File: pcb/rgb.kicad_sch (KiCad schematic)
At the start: 29 parts, among them J1 Conn_02x08_Odd_Even, J2 Conn_01x02, J3 Conn_01x02_Pin, J4 TYPE-C-31-M-12, J5 TF-01A, J6 Conn_01x02_Pin, U4 SW, U5 ESP32-WROOM-32E, U7 CH340C, U8 SPX3819M5-L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

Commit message: pcb: exploration
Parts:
- removed J3, J6: Conn_01x02_Pin, symbol Connector:Conn_01x02_Pin
- added J3, J7: B4PS-VH, Connector_PinSocket_2.54mm:PinSocket_1x04_P2.54mm_Vertical, symbol Connector:Conn_01x04_Pin
- J1: footprint Pin_Headers:Pin_Header_Angled_2x08_Pitch2.54mm -> Connector_PinSocket_2.54mm:PinSocket_2x08_P2.54mm_Vertical
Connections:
- net +5V: now also J7.1 (Pin_1), J7.2 (Pin_2)
- net GND: now also J3.3 (Pin_3), J3.4 (Pin_4), J7.3 (Pin_3), J7.4 (Pin_4)
- net Stepdown_b/v_out: now also J3.1 (Pin_1), J3.2 (Pin_2)
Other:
- moved on the sheet: C7, C8, R5, R7, U8

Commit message: initial routing done
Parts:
- removed R12: 10k, Resistors_SMD:R_0805, symbol Device:R
- removed R9: 10k, Resistor_SMD:R_0603_1608Metric, symbol Device:R
- C5: footprint Capacitors_SMD:C_0805 -> Capacitor_SMD:C_0603_1608Metric
- J2: footprint Pin_Headers:Pin_Header_Angled_1x02_Pitch2.54mm -> Connector_PinHeader_2.54mm:PinHeader_1x02_P2.54mm_Horizontal
- J5: footprint (none) -> espirgbani:TF-01A
- R4, R6: footprint Resistors_SMD:R_0805 -> Resistor_SMD:R_0603_1608Metric
- U4: value SW -> WIFI; footprint myStuff:EVQQ2 -> espirgbani:EVQQ2
- U9: footprint crtdriver2:SSOP-10-1EP_3.9x4.9mm_P1.00mm -> espirgbani:SSOP-10-1EP_3.9x4.9mm_P1.00mm
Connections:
- net USB_D_N is gone; now on net USB_N: U7.6 (UD-)
- net USB_D_P is gone; now on net USB_P: U7.5 (UD+)
- net +3.3V: now also C4.1, J2.2 (Pin_2), J5.4 (VDD)
- net +3V3: no longer C4.1, J2.1 (Pin_1), J5.4 (VDD)
- net A: now also U5.30 (IO18); no longer U5.29 (IO5)
- net B: now also U5.29 (IO5); no longer U5.30 (IO18)
- net CLK: now also U5.14 (IO12); no longer U5.36 (IO22)
- net at C5.1, R6.1, U5.4 (SENSOR_VP): now also J2.1 (Pin_1); no longer J2.2 (Pin_2)
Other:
- note added: "Light sensor ALS-PDIC144-6C/L378"
- note removed: "Photo resistor"
- moved on the sheet: J2, U4

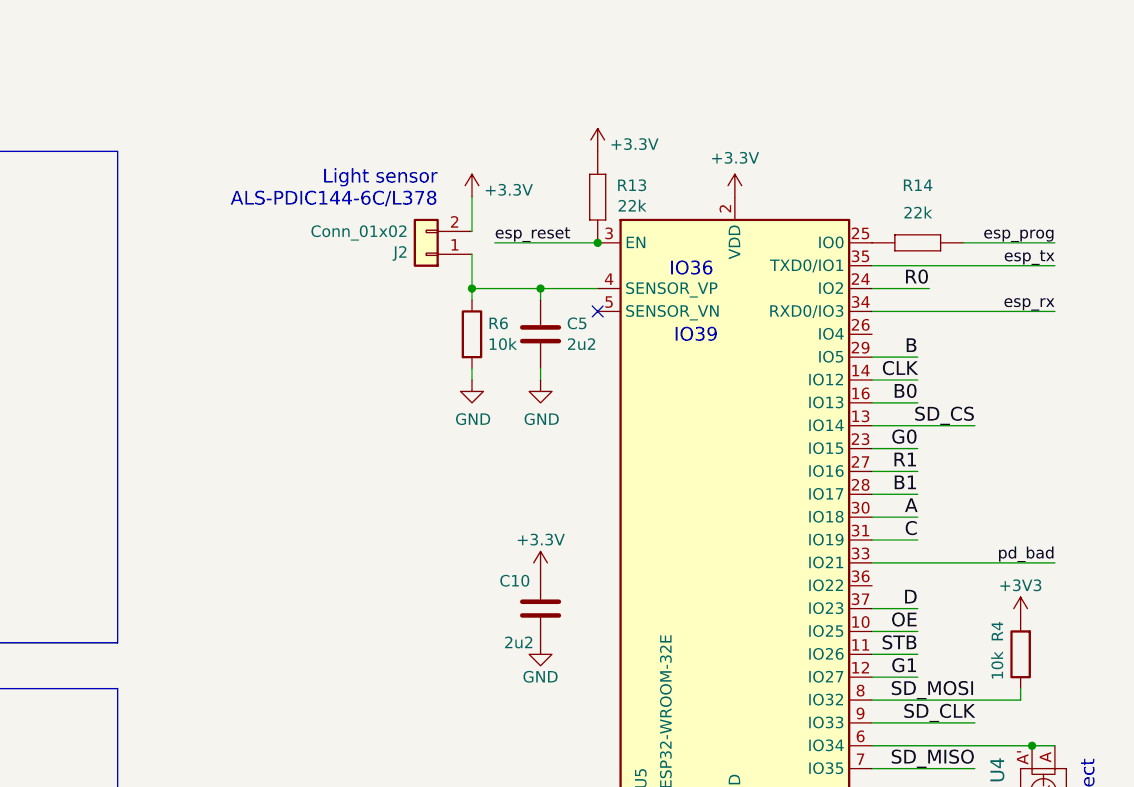
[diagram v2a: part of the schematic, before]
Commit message: turn esp by 90 deg
rip-up, re-route
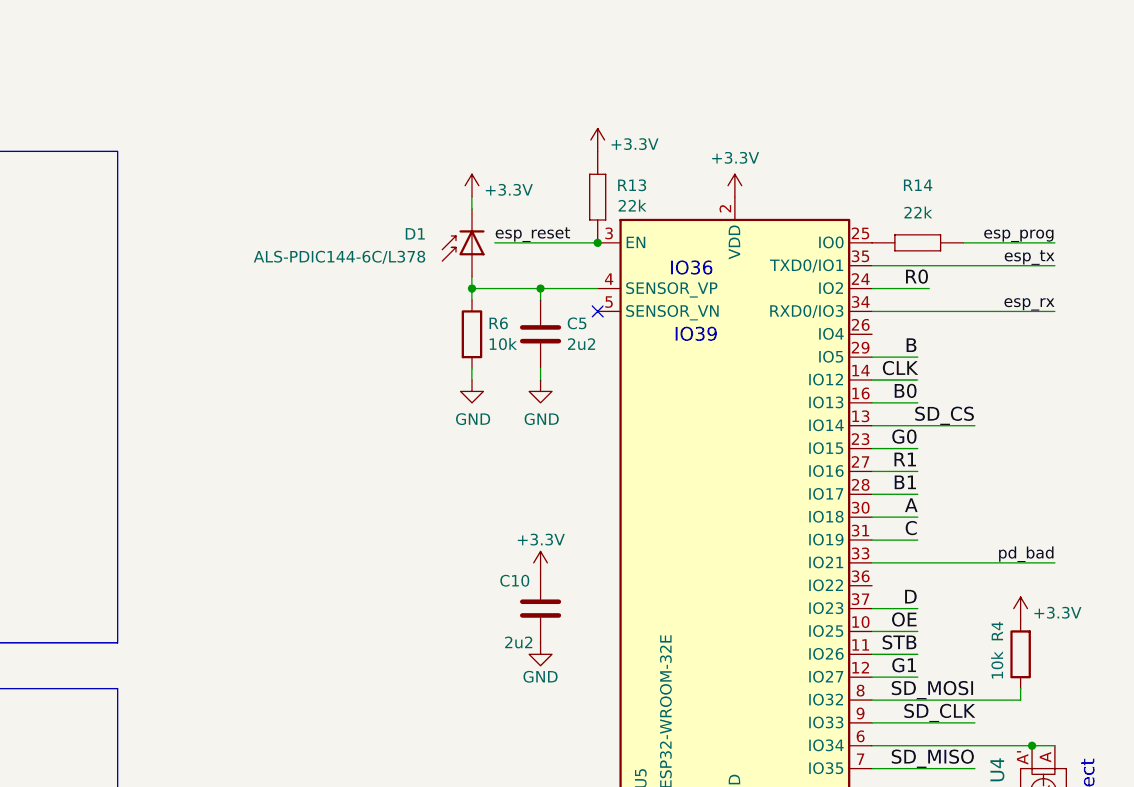
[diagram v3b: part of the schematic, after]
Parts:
- removed J2: Conn_01x02, Connector_PinHeader_2.54mm:PinHeader_1x02_P2.54mm_Horizontal, symbol Connector_Generic:Conn_01x02
- added D1: ALS-PDIC144-6C/L378, LED_THT:LED_D3.0mm_Horizontal_O3.81mm_Z6.0mm, symbol Device:D_Photo
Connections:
- net +3V3 is gone; now on net +3.3V: R4.2
- net +3.3V: now also D1.1 (K)
- net at C5.1, R6.1, U5.4 (SENSOR_VP): now also D1.2 (A)
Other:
- note removed: "Light sensor ALS-PDIC144-6C/L378"
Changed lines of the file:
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@@
 	(wire
 		(pts
-			(xy 203.2 82.55) (xy 203.2 86.36)
-		)
-		(stroke
-			(width 0)
-			(type default)
-		)
-	)
-	(wire
-		(pts
 			(xy 266.7 154.94) (xy 265.43 154.94)
 		)
@@
 	(wire
 		(pts
+			(xy 203.2 82.55) (xy 203.2 83.82)
+		)
+		(stroke
+			(width 0)
+			(type default)
+		)
+	)
+	(wire
+		(pts
 			(xy 247.65 44.45) (xy 242.57 44.45)
 		)
@@
 	(wire
 		(pts
-			(xy 203.2 88.9) (xy 203.2 92.71)
+			(xy 203.2 91.44) (xy 203.2 92.71)
 		)
 		(stroke
@@
 		)
 	)
-	(text "Light sensor\nALS-PDIC144-6C/L378"
-		(exclude_from_sim no)
-		(at 199.39 83.82 0)
-		(effects
-			(font
-				(size 1.524 1.524)
-			)
-			(justify right bottom)
-		)
-	)
 	(label "B"
 		(at 266.7 41.91 180)
@@
 	)
 	(symbol
-		(lib_id "power:+3.3V")
-		(at 264.16 129.54 0)
-		(unit 1)
-		(exclude_from_sim no)
-		(in_bom yes)
-		(on_board yes)
-		(dnp no)
-		(property "Reference" "#PWR019"
-			(at 264.16 133.35 0)
-			(effects
-				(font
-					(size 1.27 1.27)
-				)
-				(hide yes)
-			)
-		)
-		(property "Value" "+3V3"
-			(at 264.16 125.73 0)
-			(effects
-				(font
-					(size 1.27 1.27)
-				)
-			)
-		)
-		(property "Footprint" ""
-			(at 264.16 129.54 0)
-			(effects
-				(font
-					(size 1.27 1.27)
-				)
-				(hide yes)
-			)
-		)
-		(property "Datasheet" ""
-			(at 264.16 129.54 0)
-			(effects
-				(font
-					(size 1.27 1.27)
-				)
-				(hide yes)
-			)
-		)
-		(property "Description" ""
-			(at 264.16 129.54 0)
-			(effects
-				(font
-					(size 1.27 1.27)
-				)
-				(hide yes)
-			)
-		)
-		(pin "1"
-		)
-		(instances
-			(project "rgb"
-				(path "/e2cadc20-e108-4c6f-b279-00d9d28fa9da"
-					(reference "#PWR019")
-					(unit 1)
-				)
-			)
-		)
-	)
-	(symbol
 		(lib_id "rgb-rescue:TACTILE-myStuff")
 		(at 266.7 148.59 270)
@@
 	)
 	(symbol
-		(lib_id "Connector_Generic:Conn_01x02")
-		(at 198.12 88.9 180)
-		(unit 1)
-		(exclude_from_sim no)
-		(in_bom yes)
-		(on_board yes)
-		(dnp no)
-		(property "Reference" "J2"
-			(at 196.088 88.6968 0)
-			(effects
-				(font
-					(size 1.27 1.27)
-				)
-				(justify left)
-			)
-		)
-		(property "Value" "Conn_01x02"
-			(at 196.088 86.3854 0)
-			(effects
-				(font
-					(size 1.27 1.27)
-				)
-				(justify left)
-			)
-		)
-		(property "Footprint" "Connector_PinHeader_2.54mm:PinHeader_1x02_P2.54mm_Horizontal"
-			(at 198.12 88.9 0)
-			(effects
-				(font
-					(size 1.27 1.27)
-				)
-				(hide yes)
-			)
-		)
-		(property "Datasheet" ""
-			(at 198.12 88.9 0)
-			(effects
-				(font
-					(size 1.27 1.27)
-				)
-				(hide yes)
-			)
-		)
-		(property "Description" ""
-			(at 198.12 88.9 0)
-			(effects
-				(font
-					(size 1.27 1.27)
-				)
-				(hide yes)
-			)
-		)
-		(pin "1"
-		)
-		(pin "2"
-		)
-		(instances
-			(project "rgb"
-				(path "/e2cadc20-e108-4c6f-b279-00d9d28fa9da"
-					(reference "J2")
-					(unit 1)
-				)
-			)
-		)
-	)
-	(symbol
 		(lib_id "power:GND")
 		(at 133.35 95.25 0)
@@
 	)
 	(symbol
+		(lib_id "Device:D_Photo")
+		(at 203.2 88.9 90)
+		(mirror x)
+		(unit 1)
+		(exclude_from_sim no)
+		(in_bom yes)
+		(on_board yes)
+		(dnp no)
+		(property "Reference" "D1"
+			(at 198.12 86.6774 90)
+			(effects
+				(font
+					(size 1.27 1.27)
+				)
+				(justify left)
+			)
+		)
+		(property "Value" "ALS-PDIC144-6C/L378"
+			(at 198.12 89.2174 90)
+			(effects
+				(font
+					(size 1.27 1.27)
+				)
+				(justify left)
+			)
+		)
+		(property "Footprint" "LED_THT:LED_D3.0mm_Horizontal_O3.81mm_Z6.0mm"
+			(at 203.2 87.63 0)
+			(effects
+				(font
+					(size 1.27 1.27)
+				)
+				(hide yes)
+			)
+		)
+		(property "Datasheet" "~"
+			(at 203.2 87.63 0)
+			(effects
+				(font
+					(size 1.27 1.27)
+				)
+				(hide yes)
+			)
+		)
+		(property "Description" "Photodiode"
+			(at 203.2 88.9 0)
+			(effects
+				(font
+					(size 1.27 1.27)
+				)
+				(hide yes)
+			)
+		)
+		(pin "2"
+		)
+		(pin "1"
+		)
+		(instances
+			(project "rgb"
+				(path "/e2cadc20-e108-4c6f-b279-00d9d28fa9da"
+					(reference "D1")
+					(unit 1)
+				)
+			)
+		)
+	)
+	(symbol
 		(lib_id "power:+3.3V")
 		(at 203.2 82.55 0)
@@
 					(unit 1)
 				)
+			)
+		)
+	)
+	(symbol
+		(lib_id "power:+3.3V")
+		(at 264.16 129.54 0)
+		(unit 1)
+		(exclude_from_sim no)
+		(in_bom yes)
+		(on_board yes)
+		(dnp no)
+		(property "Reference" "#PWR019"
+			(at 264.16 133.35 0)
+			(effects
+				(font
+					(size 1.27 1.27)
+				)
+				(hide yes)
+			)
+		)
+		(property "Value" "+3.3V"
+			(at 268.224 128.778 0)
+			(effects
+				(font
+					(size 1.27 1.27)
+				)
+			)
+		)
+		(property "Footprint" ""
+			(at 264.16 129.54 0)
+			(effects
+				(font
+					(size 1.27 1.27)
+				)
+				(hide yes)
+			)
+		)
+		(property "Datasheet" ""
+			(at 264.16 129.54 0)
+			(effects
+				(font
+					(size 1.27 1.27)
+				)
+				(hide yes)
+			)
+		)
+		(property "Description" "Power symbol creates a global label with name \"+3.3V\""
+			(at 264.16 129.54 0)
+			(effects
+				(font
+					(size 1.27 1.27)
+				)
+				(hide yes)
+			)
+		)
+		(pin "1"
+		)
+		(instances
+			(project "rgb"
+				(path "/e2cadc20-e108-4c6f-b279-00d9d28fa9da"
+					(reference "#PWR019")
+					(unit 1)
+				)

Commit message: optimize pinout
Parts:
- C4: value 10u -> 2u2; footprint Capacitor_SMD:C_1206_3216Metric -> Capacitor_SMD:C_0603_1608Metric; JLCPN C13585 -> (none)
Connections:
- net A: now also U5.27 (IO16); no longer U5.30 (IO18)
- net B: now also U5.28 (IO17); no longer U5.29 (IO5)
- net B0: now also U5.33 (IO21); no longer U5.16 (IO13)
- net B1: now also U5.29 (IO5); no longer U5.28 (IO17)
- net C: now also U5.24 (IO2); no longer U5.31 (IO19)
- net CLK: now also U5.16 (IO13); no longer U5.14 (IO12)
- net D: now also U5.26 (IO4); no longer U5.37 (IO23)
- net G0: now also U5.37 (IO23); no longer U5.23 (IO15)
- net G1: now also U5.31 (IO19); no longer U5.12 (IO27)
- net OE: now also U5.14 (IO12); no longer U5.10 (IO25)
- net R0: now also U5.36 (IO22); no longer U5.24 (IO2)
- net R1: now also U5.30 (IO18); no longer U5.27 (IO16)
- net SD_CLK: now also U5.11 (IO26); no longer U5.9 (IO33)
- net SD_MISO: now also U5.10 (IO25); no longer U5.7 (IO35)
- net SD_MOSI: now also U5.12 (IO27); no longer U5.8 (IO32)
- net STB: now also U5.23 (IO15); no longer U5.11 (IO26)
- net pd_bad: no longer U5.33 (IO21)
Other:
- moved on the sheet: R4

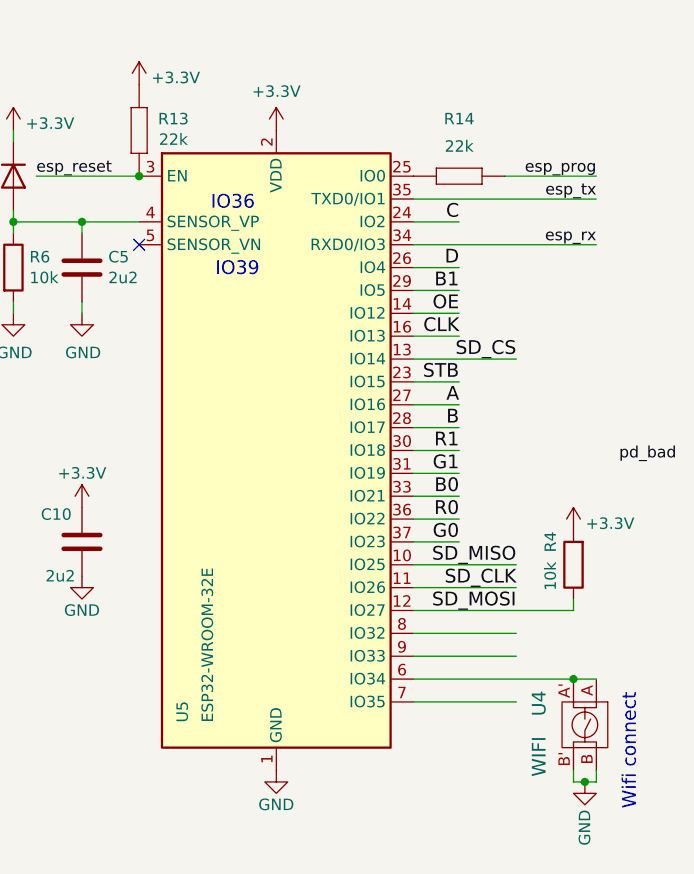
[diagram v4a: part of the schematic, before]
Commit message: put a cool pattern on the bottom silk
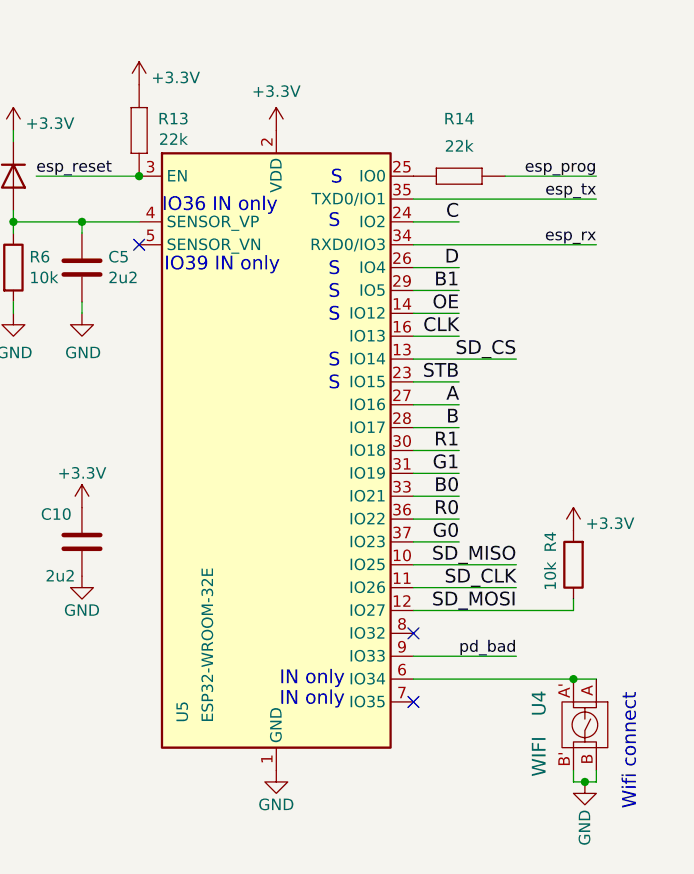
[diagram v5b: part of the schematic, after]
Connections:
- net pd_bad: now also U5.9 (IO33)
- no-connect marks 14 -> 16
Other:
- note added: "IN only"
- note added: "IO36 IN only"
- note added: "IO39 IN only"
- note added: "S"
- note removed: "IO36"
- note removed: "IO39"
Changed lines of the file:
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@@
+	)
+	(no_connect
+		(at 247.65 146.05)
 	)
 	(no_connect
@@
 	)
 	(no_connect
+		(at 247.65 138.43)
+	)
+	(no_connect
 		(at 52.07 170.18)
 	)
@@
 	(wire
 		(pts
-			(xy 247.65 138.43) (xy 259.08 138.43)
-		)
-		(stroke
-			(width 0)
-			(type default)
-		)
-	)
-	(wire
-		(pts
 			(xy 203.2 92.71) (xy 210.82 92.71)
 		)
@@
 		(pts
 			(xy 157.48 38.1) (xy 170.18 38.1)
-		)
-		(stroke
-			(width 0)
-			(type default)
-		)
-	)
-	(wire
-		(pts
-			(xy 259.08 146.05) (xy 247.65 146.05)
 		)
 		(stroke
@@
 		)
 	)
-	(text "IO36"
+	(text "IO36 IN only"
 		(exclude_from_sim no)
-		(at 227.584 90.678 0)
-		(effects
-			(font
-				(size 1.524 1.524)
-			)
+		(at 219.71 90.932 0)
+		(effects
+			(font
+				(size 1.524 1.524)
+			)
+			(justify left)
+		)
+	)
+	(text "IN only"
+		(exclude_from_sim no)
+		(at 240.03 145.796 0)
+		(effects
+			(font
+				(size 1.524 1.524)
+			)
+			(justify right)
 		)
 	)
@@
 		)
 	)
+	(text "S"
+		(exclude_from_sim no)
+		(at 239.522 108.204 0)
+		(effects
+			(font
+				(size 1.524 1.524)
+			)
+			(justify right)
+		)
+	)
 	(text "USB Power Delivery\nwith trigger IC"
 		(exclude_from_sim no)
@@
 		)
 	)
+	(text "S"
+		(exclude_from_sim no)
+		(at 239.522 92.71 0)
+		(effects
+			(font
+				(size 1.524 1.524)
+			)
+			(justify right)
+		)
+	)
 	(text "CFG1 values\n6k8	 9 V\n24k	12 V\n56k	15 V\nNC	20 V"
 		(exclude_from_sim no)
@@
 		)
 	)
-	(text "IO39"
+	(text "IO39 IN only"
 		(exclude_from_sim no)
-		(at 228.092 98.044 0)
-		(effects
-			(font
-				(size 1.524 1.524)
-			)
+		(at 219.964 97.536 0)
+		(effects
+			(font
+				(size 1.524 1.524)
+			)
+			(justify left)
 		)
 	)
@@
 		)
 	)
+	(text "S"
+		(exclude_from_sim no)
+		(at 239.522 98.044 0)
+		(effects
+			(font
+				(size 1.524 1.524)
+			)
+			(justify right)
+		)
+	)
 	(text "Wifi connect"
 		(exclude_from_sim no)
@@
 		)
 	)
+	(text "IN only"
+		(exclude_from_sim no)
+		(at 240.03 143.51 0)
+		(effects
+			(font
+				(size 1.524 1.524)
+			)
+			(justify right)
+		)
+	)
+	(text "S"
+		(exclude_from_sim no)
+		(at 239.522 100.584 0)
+		(effects
+			(font
+				(size 1.524 1.524)
+			)
+			(justify right)
+		)
+	)
+	(text "S"
+		(exclude_from_sim no)
+		(at 239.522 103.124 0)
+		(effects
+			(font
+				(size 1.524 1.524)
+			)
+			(justify right)
+		)
+	)
+	(text "S"
+		(exclude_from_sim no)
+		(at 239.522 110.744 0)
+		(effects
+			(font
+				(size 1.524 1.524)
+			)
+			(justify right)
+		)
+	)
+	(text "S"
+		(exclude_from_sim no)
+		(at 239.776 87.884 0)
+		(effects
+			(font
+				(size 1.524 1.524)
+			)
+			(justify right)
+		)
+	)
 	(label "B"
 		(at 266.7 41.91 180)
@@
 	)
 	(label "pd_bad"
-		(at 276.86 119.38 180)
-		(fields_autoplaced yes)
-		(effects
+		(at 259.08 140.97 180)
+		(fields_autoplaced yes)
+		(effects

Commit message: polish
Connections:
- net GND: no longer J1.8 (Pin_8)
- net E: now reaches U5.8 (IO32)
- net E: now also J1.8 (Pin_8)
- no-connect marks 16 -> 15
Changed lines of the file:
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@@
-	)
-	(no_connect
-		(at 247.65 138.43)
 	)
 	(no_connect
@@
 		(pts
 			(xy 133.35 151.13) (xy 143.51 151.13)
+		)
+		(stroke
+			(width 0)
+			(type default)
+		)
+	)
+	(wire
+		(pts
+			(xy 247.65 138.43) (xy 252.73 138.43)
 		)
 		(stroke
@@
 		)
 	)
+	(label "E"
+		(at 266.7 39.37 180)
+		(fields_autoplaced yes)
+		(effects
+			(font
+				(size 1.524 1.524)
+			)
+			(justify right bottom)
+		)
+	)
 	(label "C"
 		(at 242.57 44.45 0)
@@
 	(label "CLK"
 		(at 252.73 105.41 180)
+		(fields_autoplaced yes)
+		(effects
+			(font
+				(size 1.524 1.524)
+			)
+			(justify right bottom)
+		)
+	)
+	(label "E"
+		(at 252.73 138.43 180)
 		(fields_autoplaced yes)
 		(effects
@@
 					(unit 1)
 				)
-			)
-		)
-	)
-	(symbol
-		(lib_id "power:GND")
-		(at 266.7 39.37 90)
-		(unit 1)
-		(exclude_from_sim no)
-		(in_bom yes)
-		(on_board yes)
-		(dnp no)
-		(property "Reference" "#PWR016"
-			(at 273.05 39.37 0)
-			(effects
-				(font
-					(size 1.27 1.27)
-				)
-				(hide yes)
-			)
-		)
-		(property "Value" "GND"
-			(at 269.9512 39.243 90)
-			(effects
-				(font
-					(size 1.27 1.27)
-				)
-				(justify right)
-			)
-		)
-		(property "Footprint" ""
-			(at 266.7 39.37 0)
-			(effects
-				(font
-					(size 1.27 1.27)
-				)
-				(hide yes)
-			)
-		)
-		(property "Datasheet" ""
-			(at 266.7 39.37 0)
-			(effects
-				(font
-					(size 1.27 1.27)
-				)
-				(hide yes)
-			)
-		)
-		(property "Description" ""
-			(at 266.7 39.37 0)
-			(effects
-				(font
-					(size 1.27 1.27)
-				)
-				(hide yes)
-			)
-		)
-		(pin "1"
-		)
-		(instances
-			(project "rgb"
-				(path "/e2cadc20-e108-4c6f-b279-00d9d28fa9da"
-					(reference "#PWR016")
-					(unit 1)
-				)
